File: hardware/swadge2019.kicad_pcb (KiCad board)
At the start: 2 copper layers, 100 x 95.3 mm, 50 parts, among them P1 PGM, P10 CONN_1, P11 CONN_1, P12 CONN_1, P13 CONN_1, P2 USBMicroB-10118192-0001LF, P3 SAO, P7 CONN_1, P8 CONN_1, P9 CONN_1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

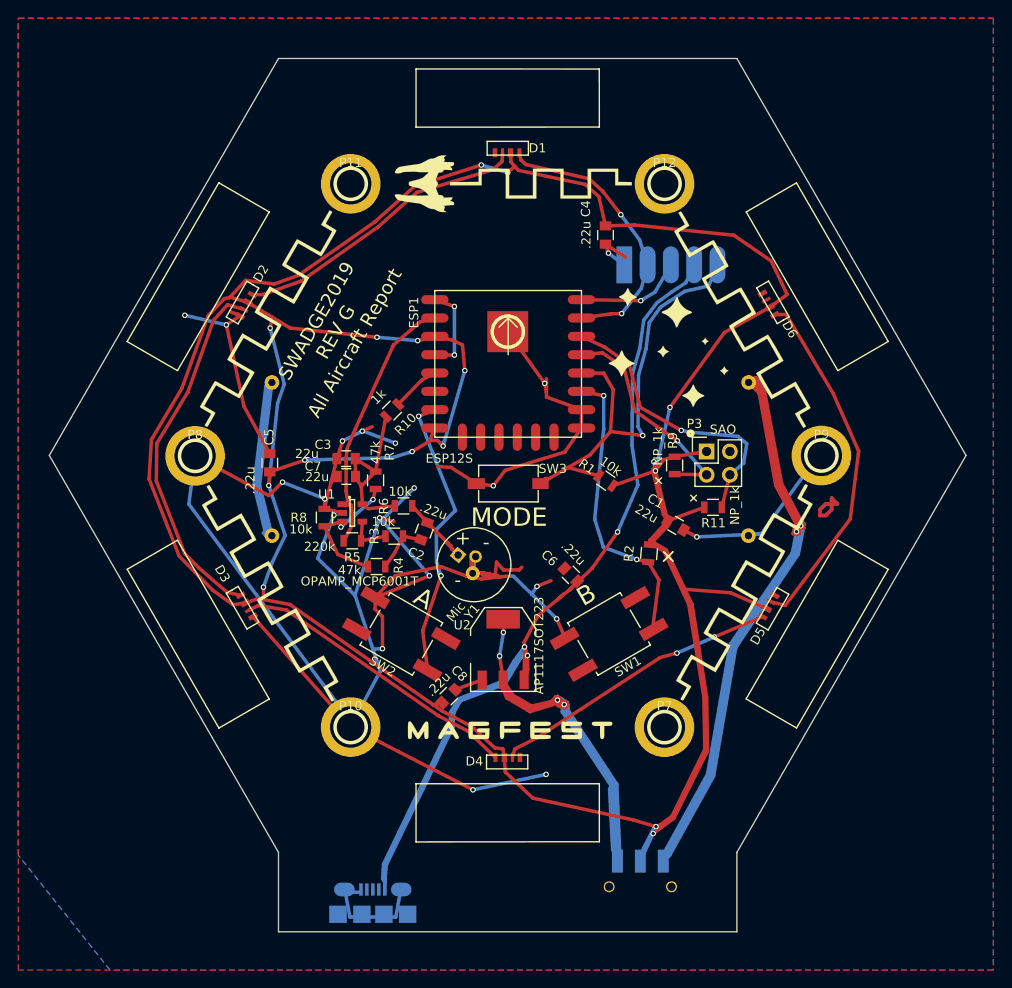
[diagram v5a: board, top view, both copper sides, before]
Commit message: Adam, this detailed commit log is for you. Update the silkscreen to Dac's wants, making it iglooized and added the numbers around the outside.
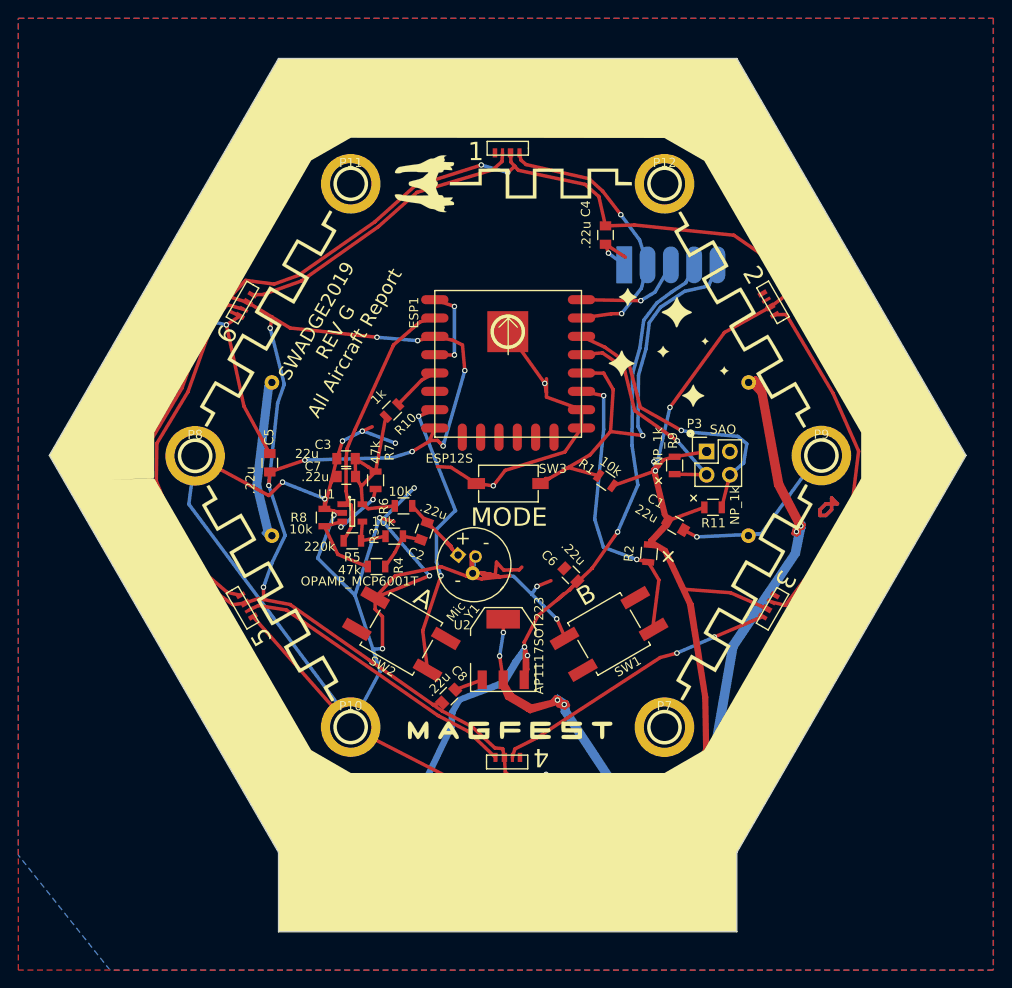
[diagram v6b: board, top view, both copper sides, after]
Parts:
- moved G*** 2.00 mm to (76.3, 109.4) (x2)
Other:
- board text added: "1"
- board text added: "2"
- board text added: "3"
- board text added: "4"
- board text added: "5"
- board text added: "6"
- board text added: "USB/OFF"
- board text removed: "USB"

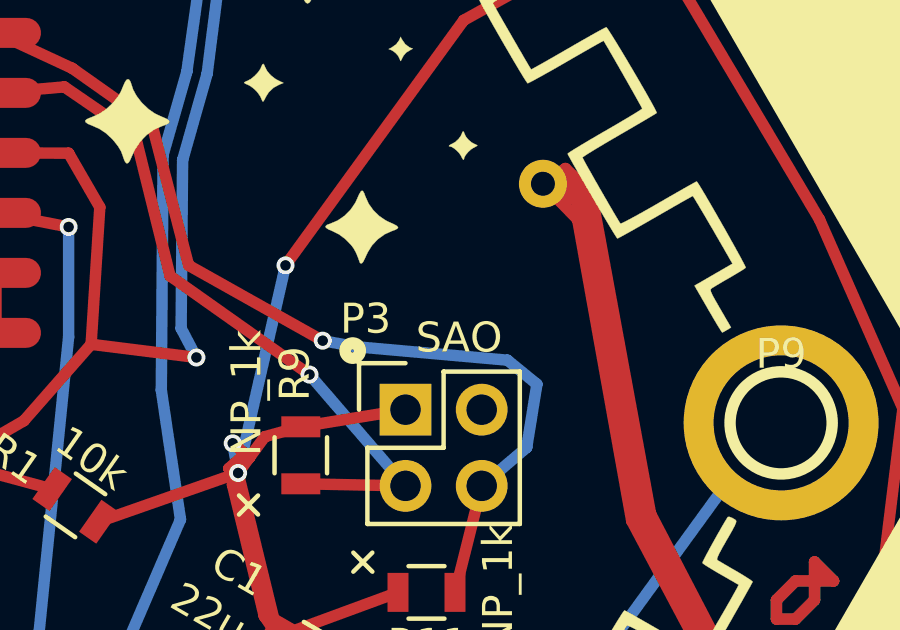
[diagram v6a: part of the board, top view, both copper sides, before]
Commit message: Update silkscreen to say "Not SAO"
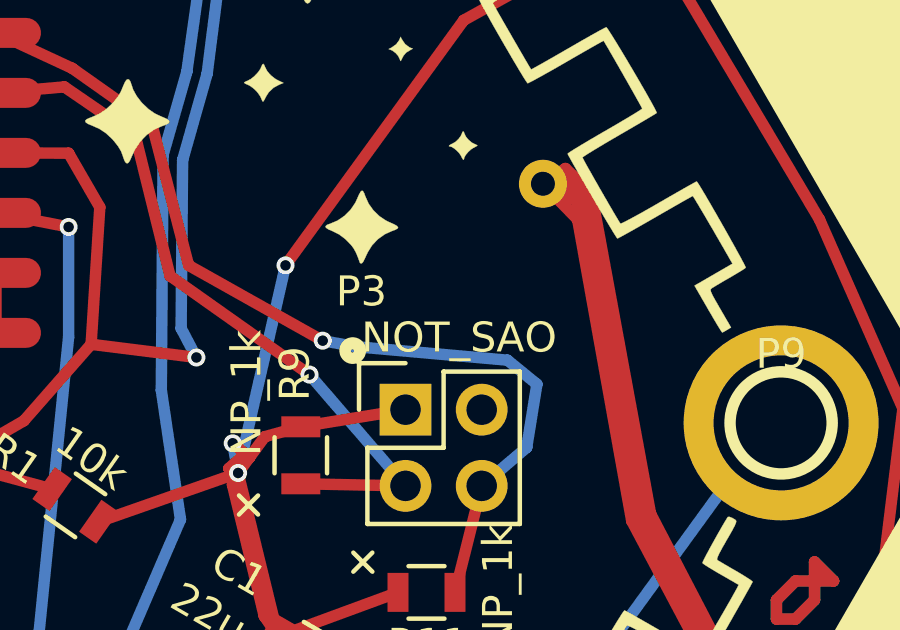
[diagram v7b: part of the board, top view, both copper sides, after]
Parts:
- P3: value SAO -> NOT_SAO
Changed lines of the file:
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@@
     (descr "Through hole pin header")
     (tags "pin header")
-    (fp_text reference P3 (at -1.33 -3.03) (layer F.SilkS)
+    (fp_text reference P3 (at -1.47 -3.94) (layer F.SilkS)
       (effects (font (size 1 1) (thickness 0.15)))
     )
-    (fp_text value SAO (at 1.786 -2.402) (layer F.SilkS)
+    (fp_text value NOT_SAO (at 1.786 -2.402) (layer F.SilkS)
       (effects (font (size 1 1) (thickness 0.15)))
     )

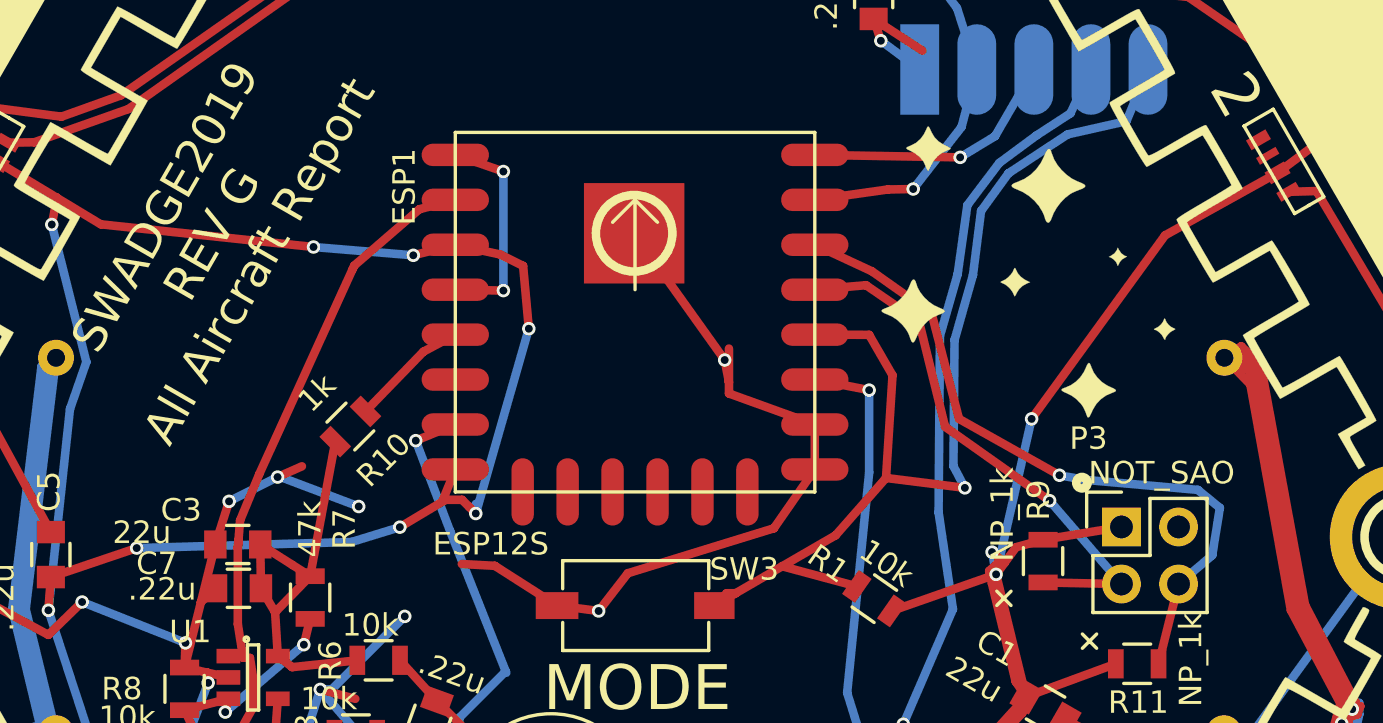
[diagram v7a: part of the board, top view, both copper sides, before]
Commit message: Update with rev H - fixed SAO
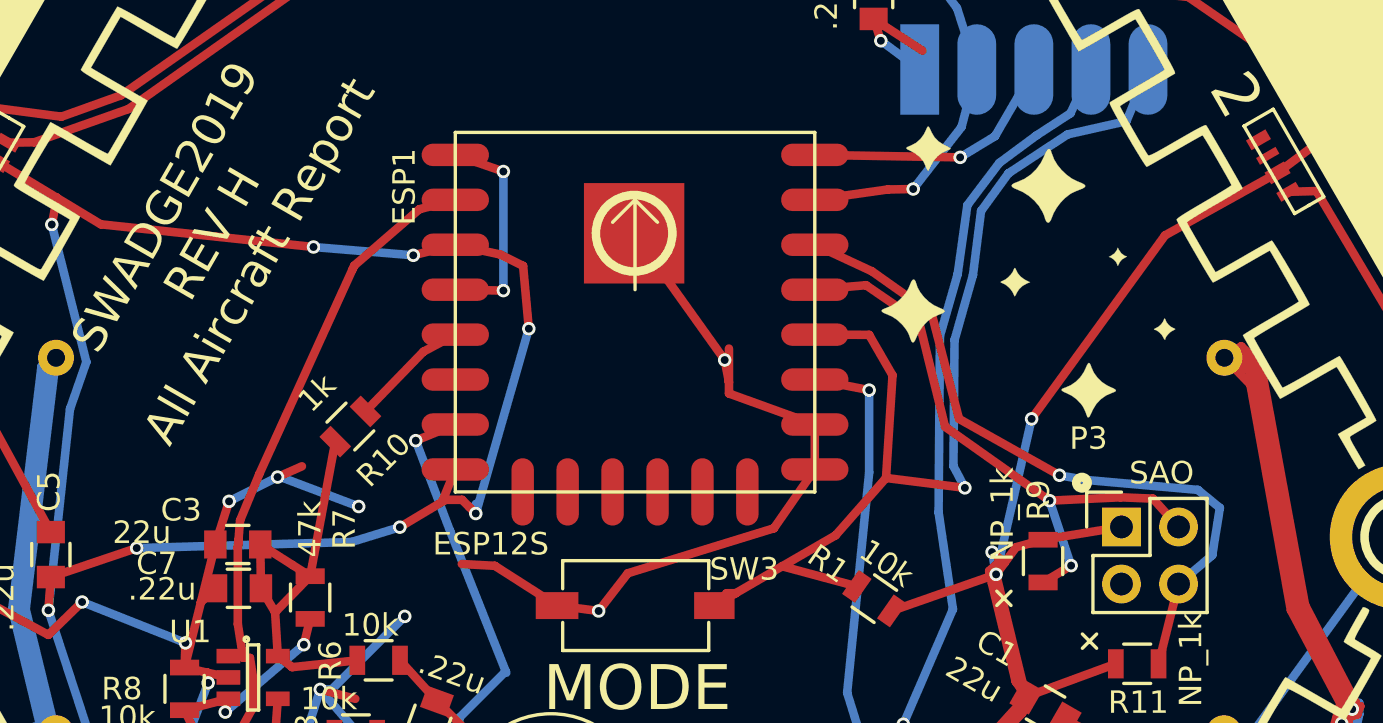
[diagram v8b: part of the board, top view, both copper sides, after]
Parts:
- P3: value NOT_SAO -> SAO
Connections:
- P3 pad 2: GND -> GPIO4
- P3 pad 3: GPIO4 -> GND
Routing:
- net GPIO4: track 24.1 -> 26.5 mm, vias 1 -> 2
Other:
- board text added: "SWADGE2019 REV H All Aircraft Report"
- board text removed: "SWADGE2019 REV G All Aircraft Report"
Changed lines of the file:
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@@
     (thickness 1.6)
     (drawings 133)
-    (tracks 613)
+    (tracks 617)
     (zones 0)
     (modules 50)
@@
       (drillshape 0)
       (scaleselection 1)
-      (outputdirectory swadge2019-revG))
+      (outputdirectory swadge2019-revH))
   )
   (net 0 "")
@@
       (effects (font (size 1 1) (thickness 0.15)))
     )
-    (fp_text value NOT_SAO (at 1.786 -2.402) (layer F.SilkS)
+    (fp_text value SAO (at 1.786 -2.402) (layer F.SilkS)
       (effects (font (size 1 1) (thickness 0.15)))
     )
@@
       (net 1 +3V3))
     (pad 2 thru_hole oval (at 2.54 0) (size 1.7272 1.7272) (drill 1.016) (layers *.Cu *.Mask F.SilkS)
-      (net 2 GND))
-    (pad 3 thru_hole oval (at 0 2.54) (size 1.7272 1.7272) (drill 1.016) (layers *.Cu *.Mask F.SilkS)
       (net 16 GPIO4))
+    (pad 3 thru_hole oval (at 0 2.54) (size 1.7272 1.7272) (drill 1.016) (layers *.Cu *.Mask F.SilkS)
+      (net 2 GND))
     (pad 4 thru_hole oval (at 2.54 2.54) (size 1.7272 1.7272) (drill 1.016) (layers *.Cu *.Mask F.SilkS)
       (net 26 GPIO5))
@@
     (effects (font (size 1.5 1.5) (thickness 0.3)) (justify mirror))
   )
-  (gr_text "SWADGE2019\nREV G\nAll Aircraft Report" (at 57.43 62.73 60) (layer F.SilkS)
+  (gr_text "SWADGE2019\nREV H\nAll Aircraft Report" (at 57.43 62.73 60) (layer F.SilkS)
     (effects (font (size 1.5 1.5) (thickness 0.3)))
   )
@@
   (segment (start 87.71 69.02) (end 86.67 67.22) (width 0.381) (layer F.Cu) (net 15))
   (segment (start 86.67 67.22) (end 84.25 67.21) (width 0.381) (layer F.Cu) (net 15))
-  (segment (start 97.9 78.31) (end 94.7 74.6) (width 0.381) (layer B.Cu) (net 16))
+  (segment (start 94.41 78.24) (end 95.66 77.49) (width 0.381) (layer F.Cu) (net 16))
+  (via (at 95.66 77.49) (size 0.6) (drill 0.35) (layers F.Cu B.Cu) (net 16))
+  (segment (start 95.66 77.49) (end 94.7 74.6) (width 0.381) (layer B.Cu) (net 16))
+  (segment (start 100.44 75.77) (end 99.3 74.51) (width 0.381) (layer F.Cu) (net 16))
+  (segment (start 99.3 74.51) (end 97.86 74.45) (width 0.381) (layer F.Cu) (net 16))
+  (segment (start 97.86 74.45) (end 94.7 74.6) (width 0.381) (layer F.Cu) (net 16))
   (via (at 94.7 74.6) (size 0.6) (drill 0.35) (layers F.Cu B.Cu) (net 16))
   (segment (start 94.7 74.6) (end 90.05 71.31) (width 0.381) (layer F.Cu) (net 16))
@@
   (segment (start 88.89 66.63) (end 86.53 65.01) (width 0.381) (layer F.Cu) (net 16))
   (segment (start 86.53 65.01) (end 84.25 65.21) (width 0.381) (layer F.Cu) (net 16))
-  (segment (start 97.9 78.31) (end 94.41 78.24) (width 0.381) (layer F.Cu) (net 16))
   (segment (start 60.2 85.516) (end 62.872 85.008) (width 0.381) (layer F.Cu) (net 17))
   (segment (start 60.2 85.516) (end 60.35 83.418) (width 0.381) (layer F.Cu) (net 17))
